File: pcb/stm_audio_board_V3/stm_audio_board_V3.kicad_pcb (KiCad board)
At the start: 4 copper layers, 66.1 x 71 mm, 152 parts, among them J1 Power conn, J2 STlink, J3 Audio_sig, J4 Conn_01x01_taptempo, J6 Conn_01x03_pot_ext, SW1 SW_SPST, U1 AS4C4M16SA, U2 OP275, U3 MP-K7805-500R3, U4 OP275, U5 MIC2920A-3.3WS-TR, U6 L7809, U7 STM32H723ZGTx, U9 MIC2920A-3.3WS-TR, Y2 X1E0000210132

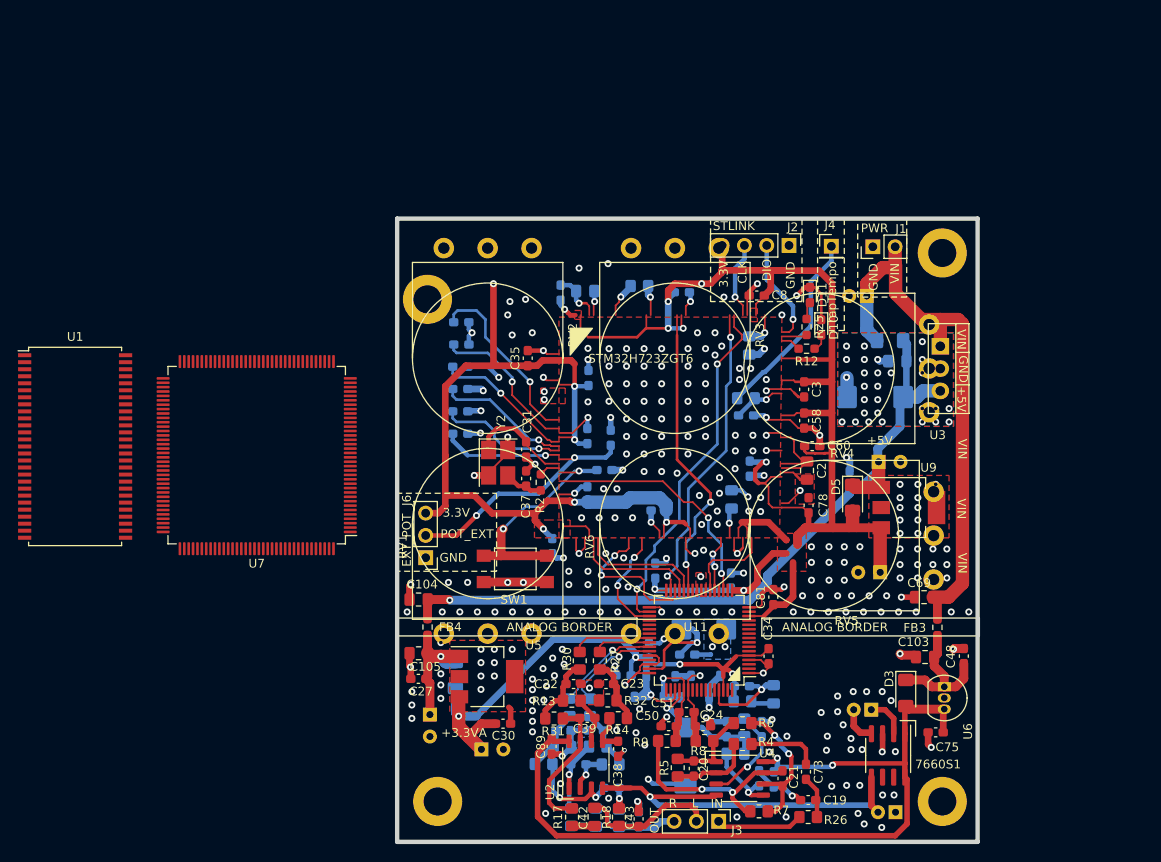
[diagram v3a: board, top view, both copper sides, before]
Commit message: v3 pcb updated pinout generated form cubeide
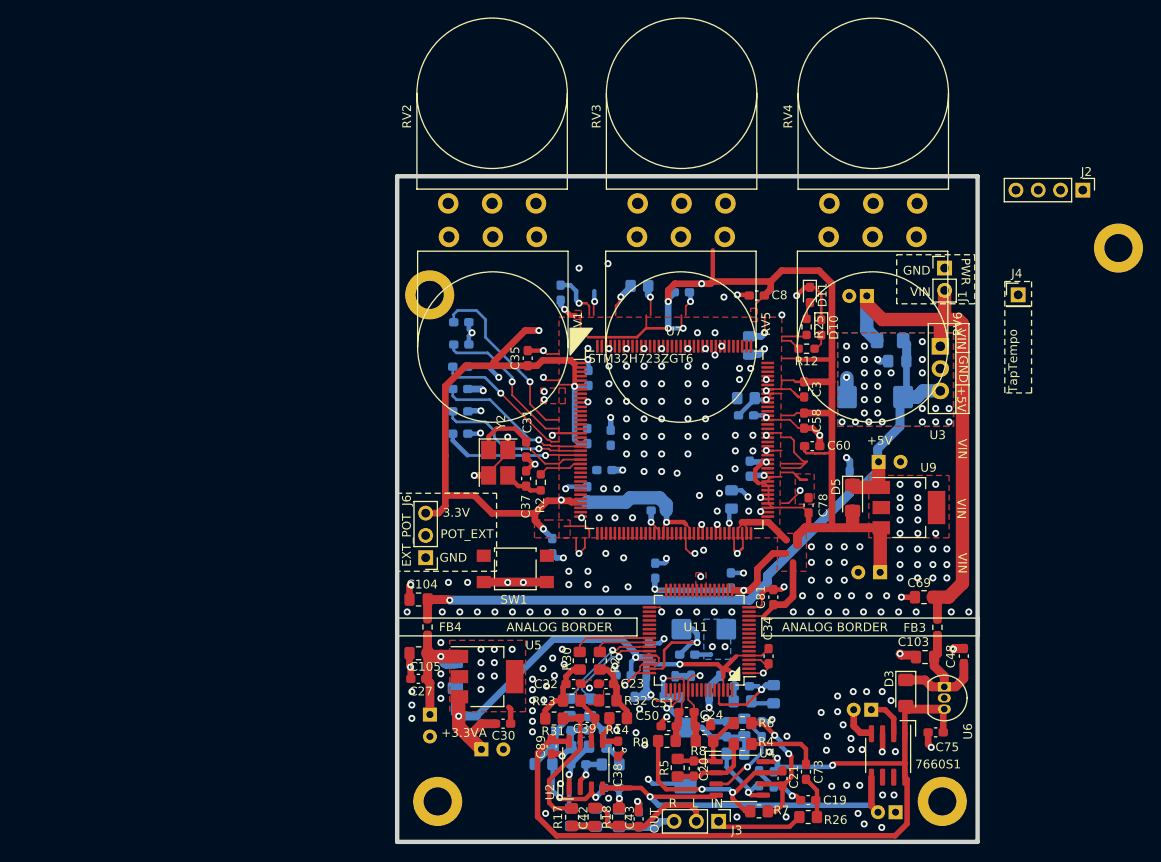
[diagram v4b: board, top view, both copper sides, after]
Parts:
- removed C2, C52: 2.2uF, Capacitor_SMD:C_0805_2012Metric_Pad1.18x1.45mm_HandSolder
- removed U1: AS4C4M16SA, Package_SO:TSOP-II-54_22.2x10.16mm_P0.8mm
- moved U7 47.6 mm to (214.5, 71.1), turned to 0 degrees
- moved RV6 46.9 mm to (232.2, 48.0), turned to -90 degrees
- moved RV1 46.2 mm to (188.9, 48.0), turned to -90 degrees
- moved RV5 44.6 mm to (210.3, 48.0), turned to -90 degrees
- moved J2 34.1 mm to (261.1, 42.7)
- moved J4 22.0 mm to (253.7, 54.6)
- moved H3 20.1 mm to (265.2, 49.3)
- moved RV4 13.9 mm to (242.2, 44.2), turned to 90 degrees
- moved RV3 11.9 mm to (220.4, 44.2), turned to 90 degrees
- moved RV2 11.7 mm to (198.8, 44.2), turned to 90 degrees
- moved J1 8.53 mm to (245.4, 51.6), turned to 0 degrees
- moved H4 0.57 mm to (186.7, 54.6)
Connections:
- C1 pad 1: unconnected-(C1-Pad1) -> Net-(C1-Pad1)
- C49 pad 1: unconnected-(C49-Pad1) -> Net-(C49-Pad1)
- R1 pad 1: unconnected-(R1-Pad1) -> Net-(U7-BOOT0)
- U7 pad 106: unconnected-(U7-VCAP-Pad106) -> Net-(C49-Pad1)
- U7 pad 107: Net-(U7-VSS-Pad107) -> GND
- U7 pad 108: unconnected-(U7-VDD-Pad108) -> +3.3V
- U7 pad 111: unconnected-(U7-PC10-Pad111) -> AD1939_I2S2_CK
- U7 pad 120: Net-(U7-VSS-Pad107) -> GND
- U7 pad 121: unconnected-(U7-VDD-Pad121) -> +3.3V
- U7 pad 13: unconnected-(U7-PF3-Pad13) -> POT1
- U7 pad 130: Net-(U7-VSS-Pad107) -> GND
- U7 pad 131: unconnected-(U7-VDD-Pad131) -> +3.3V
- U7 pad 138: unconnected-(U7-BOOT0-Pad138) -> Net-(U7-BOOT0)
- U7 pad 143: unconnected-(U7-PDR_ON-Pad143) -> GND
- U7 pad 144: unconnected-(U7-VDD-Pad144) -> +3.3V
- U7 pad 15: unconnected-(U7-PF5-Pad15) -> POT2
- U7 pad 16: Net-(U7-VSS-Pad107) -> GND
- U7 pad 17: unconnected-(U7-VDD-Pad17) -> +3.3V
- U7 pad 19: unconnected-(U7-PF7-Pad19) -> POT3
- U7 pad 20: unconnected-(U7-PF8-Pad20) -> POT4
- U7 pad 21: unconnected-(U7-PF9-Pad21) -> POT5
- U7 pad 22: unconnected-(U7-PF10-Pad22) -> POT6
- U7 pad 23: unconnected-(U7-PH0-Pad23) -> OSC0
- U7 pad 24: unconnected-(U7-PH1-Pad24) -> OSC1
- U7 pad 25: unconnected-(U7-NRST-Pad25) -> /MCU/NRST
- U7 pad 28: unconnected-(U7-PC2_C-Pad28) -> AD1939_I2S1_SDI
- U7 pad 30: unconnected-(U7-VDD-Pad30) -> +3.3V
- U7 pad 31: unconnected-(U7-VSSA-Pad31) -> GND
- U7 pad 32: unconnected-(U7-VREF+-Pad32) -> +3.3V
- U7 pad 33: unconnected-(U7-VDDA-Pad33) -> +3.3V
- U7 pad 38: Net-(U7-VSS-Pad107) -> GND
- U7 pad 39: unconnected-(U7-VDD-Pad39) -> +3.3V
- U7 pad 40: unconnected-(U7-PA4-Pad40) -> AD1939_I2S2_WS
- U7 pad 41: unconnected-(U7-PA5-Pad41) -> AD1939_SPI3_CLK
- U7 pad 42: unconnected-(U7-PA6-Pad42) -> AD1939_SPI3_MISO
- U7 pad 43: unconnected-(U7-PA7-Pad43) -> AD1939_SPI3_MOSI
- U7 pad 48: unconnected-(U7-PB2-Pad48) -> AD1939_I2S2_SDO
- U7 pad 51: Net-(U7-VSS-Pad107) -> GND
- U7 pad 52: unconnected-(U7-VDD-Pad52) -> +3.3V
- U7 pad 6: unconnected-(U7-VBAT-Pad6) -> +3.3V
- U7 pad 61: Net-(U7-VSS-Pad107) -> GND
- U7 pad 62: unconnected-(U7-VDD-Pad62) -> +3.3V
- U7 pad 69: unconnected-(U7-PB10-Pad69) -> AD1939_I2S1_CK
- U7 pad 71: unconnected-(U7-VCAP-Pad71) -> Net-(C1-Pad1)
- U7 pad 72: unconnected-(U7-VDD-Pad72) -> +3.3V
- U7 pad 73: unconnected-(U7-PB12-Pad73) -> AD1939_I2S1_WS
- U7 pad 83: Net-(U7-VSS-Pad107) -> GND
- U7 pad 84: unconnected-(U7-VDD-Pad84) -> +3.3V
- U7 pad 94: Net-(U7-VSS-Pad107) -> GND
- U7 pad 95: unconnected-(U7-VDD33USB-Pad95) -> +3.3V
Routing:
- net AD1939_SPI3_CLK: track 40.3 -> 0.00 mm, vias 2 -> 0
- net AD1939_SPI3_MISO: track 34.6 -> 0.00 mm, vias 2 -> 0
- net AD1939_I2S1_SDI: track 34.2 -> 0.00 mm, vias 2 -> 0
- net AD1939_I2S2_SDO: track 27.7 -> 0.00 mm, vias 2 -> 0
- net POT_EXT: track 27.7 -> 0.00 mm, vias 2 -> 0
- net /MCU/NRST: track 26.0 -> 0.00 mm, vias 2 -> 0
- net TAP_TEMPO_INPUT: track 21.9 -> 0.00 mm
- net AD1939_SPI3_MOSI: track 17.4 -> 0.00 mm, vias 2 -> 0
- net AD1939_I2S1_WS: track 14.4 -> 0.00 mm
- net AD1939_I2S1_CK: track 14.4 -> 0.00 mm
- net (no net): track 3.92 -> 17.8 mm, vias 0 -> 1
- net AD1939_SPI_CS: track 12.5 -> 0.00 mm, vias 2 -> 0
- net SWDIO: track 12.2 -> 0.00 mm, vias 1 -> 0
- net GND: track 198.4 -> 187.2 mm, vias 312 -> 305
- net /MCU/VDD_DSI: track 11.0 -> 0.00 mm
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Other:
- board size 66.1 x 71 mm -> 66.1 x 75.8 mm
- board text removed: "CLK"
- board text removed: "DIO"
- board text removed: "STLINK"
